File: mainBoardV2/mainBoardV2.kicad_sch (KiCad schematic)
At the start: 33 parts, among them J1 USB4125-GF-A_REVA2, SW1 SW_SPST, U1 ESP32-CAM, U2 ESP32-DEVKITC-32E, U3 MCP73871-2AAI_ML, U4 MPU6050_Module, U5 TPS61090RSARG4

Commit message: 3.6.26.C1
Wanted to start, but ended this session early
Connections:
- net +5V: no longer C4.1, R6.1, U3.17 (CE), U3.18 (IN), U3.19 (IN), U3.3 (SEL), U3.4 (PROG2), U3.9 (~{TE}), U7.4 (Common_Anode)
- net GND: no longer U6.2 (VBAT-)
- net at C6.1, U3.14 (VBAT), U3.15 (VBAT)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: no longer C1.1, L1.2, R1.1, U5.11 (EN), U5.8 (VBAT)
- new net: RintoCam1.2, RintoGyro1.2, SW1.1 (A), U2.J2_19 (EXT_5V)
- new net: C2.1, C3.1, R3.2, R5.1, U5.1 (VOUT), U5.15 (VOUT)
- new net: C1.1, L1.2, R1.1, U5.11 (EN), U5.8 (VBAT)
- new net: C4.1, R6.1, U3.17 (CE), U3.18 (IN), U3.19 (IN), U3.3 (SEL), U3.4 (PROG2), U3.9 (~{TE}), U7.4 (Common_Anode)
- new net: C5.1, U3.1 (OUT), U3.20 (OUT)
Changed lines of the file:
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@@
-	)
-	(junction
-		(at 160.02 62.23)
-		(diameter 0)
-		(color 0 0 0 0)
 	)
 	(junction
@@
 	)
 	(junction
-		(at 68.58 101.6)
-		(diameter 0)
-		(color 0 0 0 0)
-	)
-	(junction
 		(at 187.96 83.82)
 		(diameter 0)
@@
 	(junction
 		(at 115.57 156.21)
-		(diameter 0)
-		(color 0 0 0 0)
-	)
-	(junction
-		(at 41.91 167.64)
 		(diameter 0)
 		(color 0 0 0 0)
@@
 	(wire
 		(pts
-			(xy 154.94 156.21) (xy 154.94 62.23)
-		)
-		(stroke
-			(width 0)
-			(type default)
-		)
-	)
-	(wire
-		(pts
 			(xy 195.58 77.47) (xy 195.58 128.27)
 		)
@@
 	(wire
 		(pts
-			(xy 68.58 91.44) (xy 17.78 91.44)
-		)
-		(stroke
-			(width 0)
-			(type default)
-		)
-	)
-	(wire
-		(pts
 			(xy 73.66 114.3) (xy 76.2 114.3)
 		)
@@
 	(wire
 		(pts
-			(xy 68.58 101.6) (xy 76.2 101.6)
-		)
-		(stroke
-			(width 0)
-			(type default)
-		)
-	)
-	(wire
-		(pts
 			(xy 110.49 26.67) (xy 148.59 26.67)
 		)
@@
 	(wire
 		(pts
-			(xy 68.58 101.6) (xy 68.58 91.44)
-		)
-		(stroke
-			(width 0)
-			(type default)
-		)
-	)
-	(wire
-		(pts
 			(xy 185.42 67.31) (xy 195.58 67.31)
 		)
@@
 	(wire
 		(pts
-			(xy 21.59 167.64) (xy 41.91 167.64)
-		)
-		(stroke
-			(width 0)
-			(type default)
-		)
-	)
-	(wire
-		(pts
 			(xy 243.84 38.1) (xy 243.84 44.45)
 		)
@@
 	(wire
 		(pts
-			(xy 160.02 26.67) (xy 160.02 62.23)
-		)
-		(stroke
-			(width 0)
-			(type default)
-		)
-	)
-	(wire
-		(pts
 			(xy 110.49 33.02) (xy 134.62 33.02)
 		)
@@
 	(wire
 		(pts
-			(xy 17.78 91.44) (xy 17.78 26.67)
-		)
-		(stroke
-			(width 0)
-			(type default)
-		)
-	)
-	(wire
-		(pts
 			(xy 139.7 156.21) (xy 146.05 156.21)
 		)
@@
 	(wire
 		(pts
-			(xy 62.23 101.6) (xy 68.58 101.6)
+			(xy 62.23 101.6) (xy 76.2 101.6)
 		)
 		(stroke
@@
 	(wire
 		(pts
-			(xy 154.94 62.23) (xy 160.02 62.23)
-		)
-		(stroke
-			(width 0)
-			(type default)
-		)
-	)
-	(wire
-		(pts
 			(xy 74.93 60.96) (xy 74.93 64.77)
 		)
@@
 	(wire
 		(pts
-			(xy 41.91 120.65) (xy 41.91 160.02)
-		)
-		(stroke
-			(width 0)
-			(type default)
-		)
-	)
-	(wire
-		(pts
 			(xy 58.42 152.4) (xy 58.42 160.02)
 		)
@@
 	(wire
 		(pts
-			(xy 160.02 62.23) (xy 172.72 62.23)
-		)
-		(stroke
+			(xy 154.94 62.23) (xy 172.72 62.23)
+		)
+		(stroke

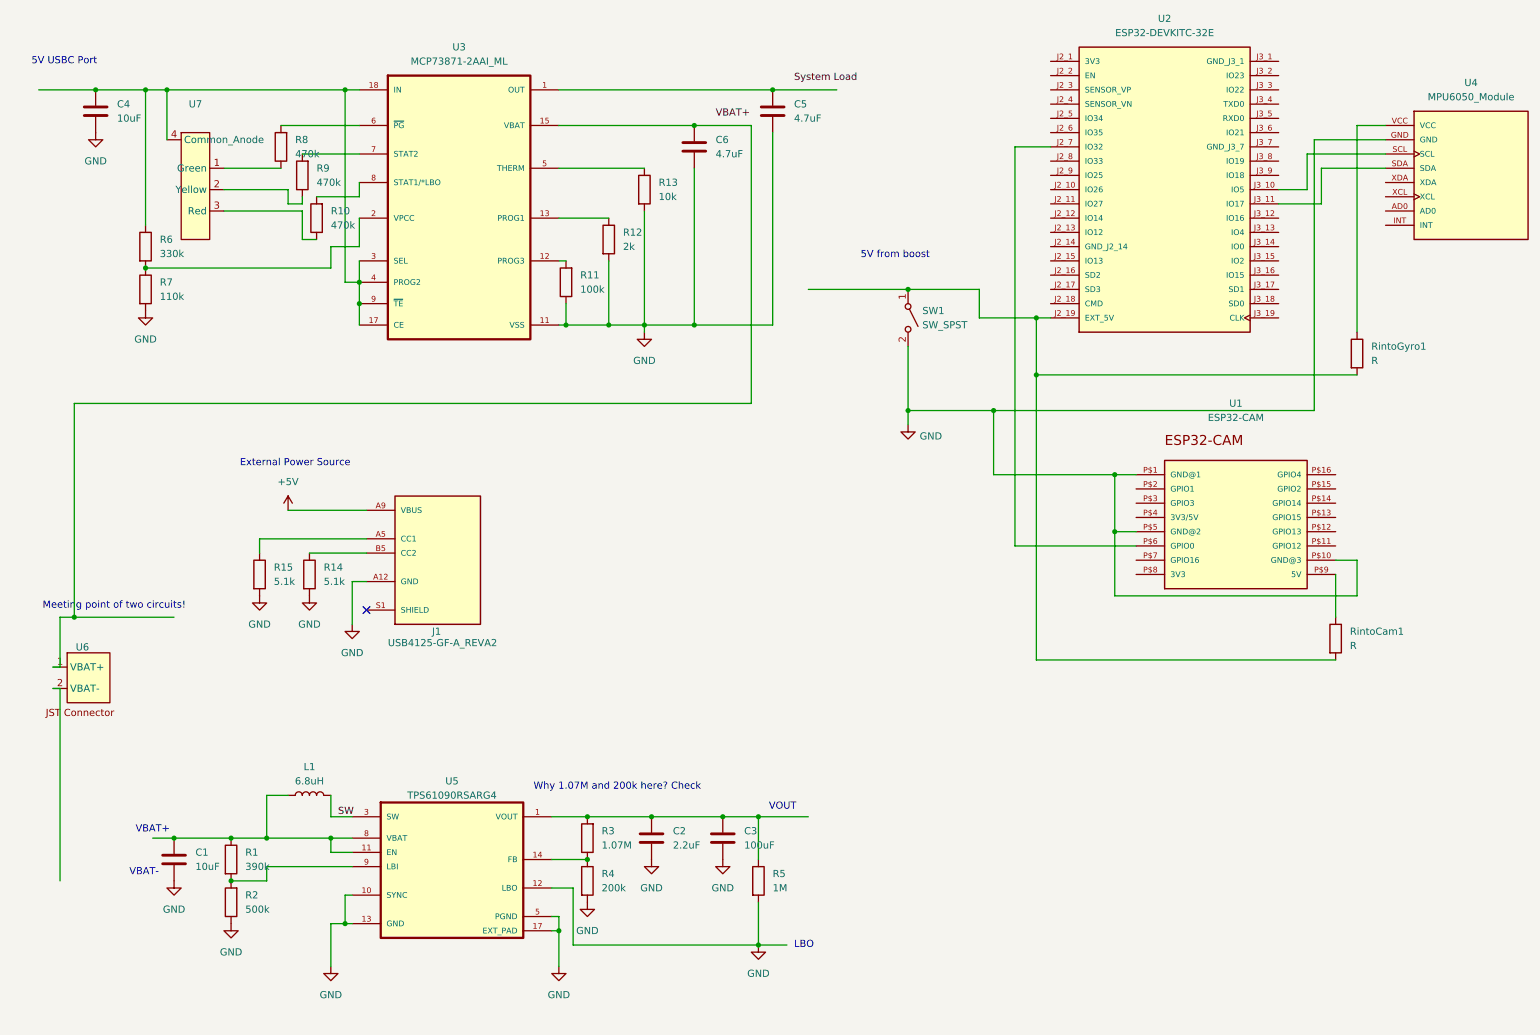
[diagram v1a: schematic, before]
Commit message: 3.7.26.C1
removed the old boost converter chip and circuit and put in the new one. Unconnected.
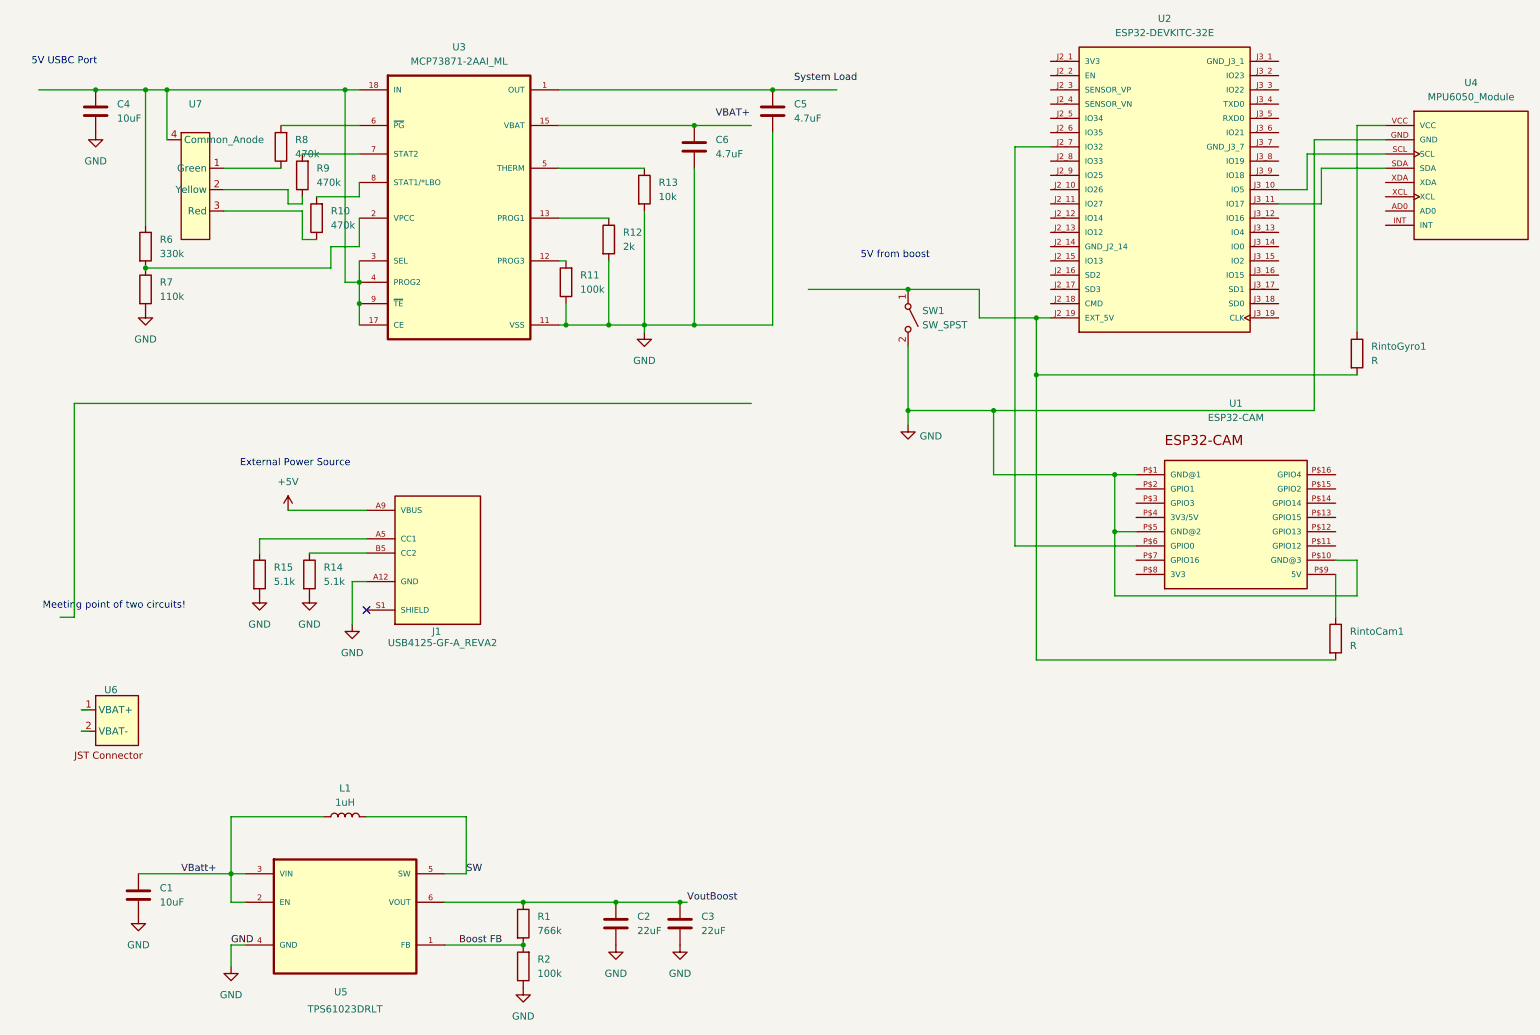
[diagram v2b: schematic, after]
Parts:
- removed R3: 1.07M, Resistor_SMD:R_0805_2012Metric_Pad1.20x1.40mm_HandSolder, symbol Device:R
- removed R4: 200k, Resistor_SMD:R_0805_2012Metric_Pad1.20x1.40mm_HandSolder, symbol Device:R
- removed R5: 1M, Resistor_SMD:R_0805_2012Metric_Pad1.20x1.40mm_HandSolder, symbol Device:R
- removed U5: TPS61090RSARG4, TPS61090RSARG4:QFN65P400X400X100-17N, symbol TPS61090RSARG4:TPS61090RSARG4
- added U5: TPS61023DRLT, TPS61023DRLT:SOT50P160X60-6N, symbol TPS61023DRLT:TPS61023DRLT
- C2: value 2.2uF -> 22uF
- C3: value 100uF -> 22uF; footprint T495C107K006ATE150(1):CAPMP6032X250 -> Capacitor_SMD:C_0805_2012Metric_Pad1.18x1.45mm_HandSolder
- L1: value 6.8uH -> 1uH
- R1: value 390k -> 766k
- R2: value 500k -> 100k
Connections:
- net GND: now also U5.4 (GND)
- net SW: now also U5.5 (SW)
- net at C6.1, U3.14 (VBAT), U3.15 (VBAT)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: no longer U6.1 (VBAT+)
- net VoutBoost: now reaches C2.1, C3.1
- net VoutBoost: now also R1.1, U5.6 (VOUT)
- net VBatt+: now reaches C1.1, L1.2
- net VBatt+: now also U5.2 (EN), U5.3 (VIN); no longer R1.1
- net Boost FB: now reaches R1.2, R2.2
- net Boost FB: now also U5.1 (FB)
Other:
- note removed: "LBO"
- note removed: "VBAT+"
- note removed: "VBAT-"
- note removed: "VOUT"
- note removed: "Why 1.07M and 200k here? Check"
- moved on the sheet: C1, C2, L1, R1, R2, U6

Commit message: 3.9.26.Cf
Closing the 3.9 session as it ran into 3.10. boost circuit ready to be optimally connected.

Charger ready for a fresh start.

Warning about 3 unconnected vias currently. Don't see them yet.
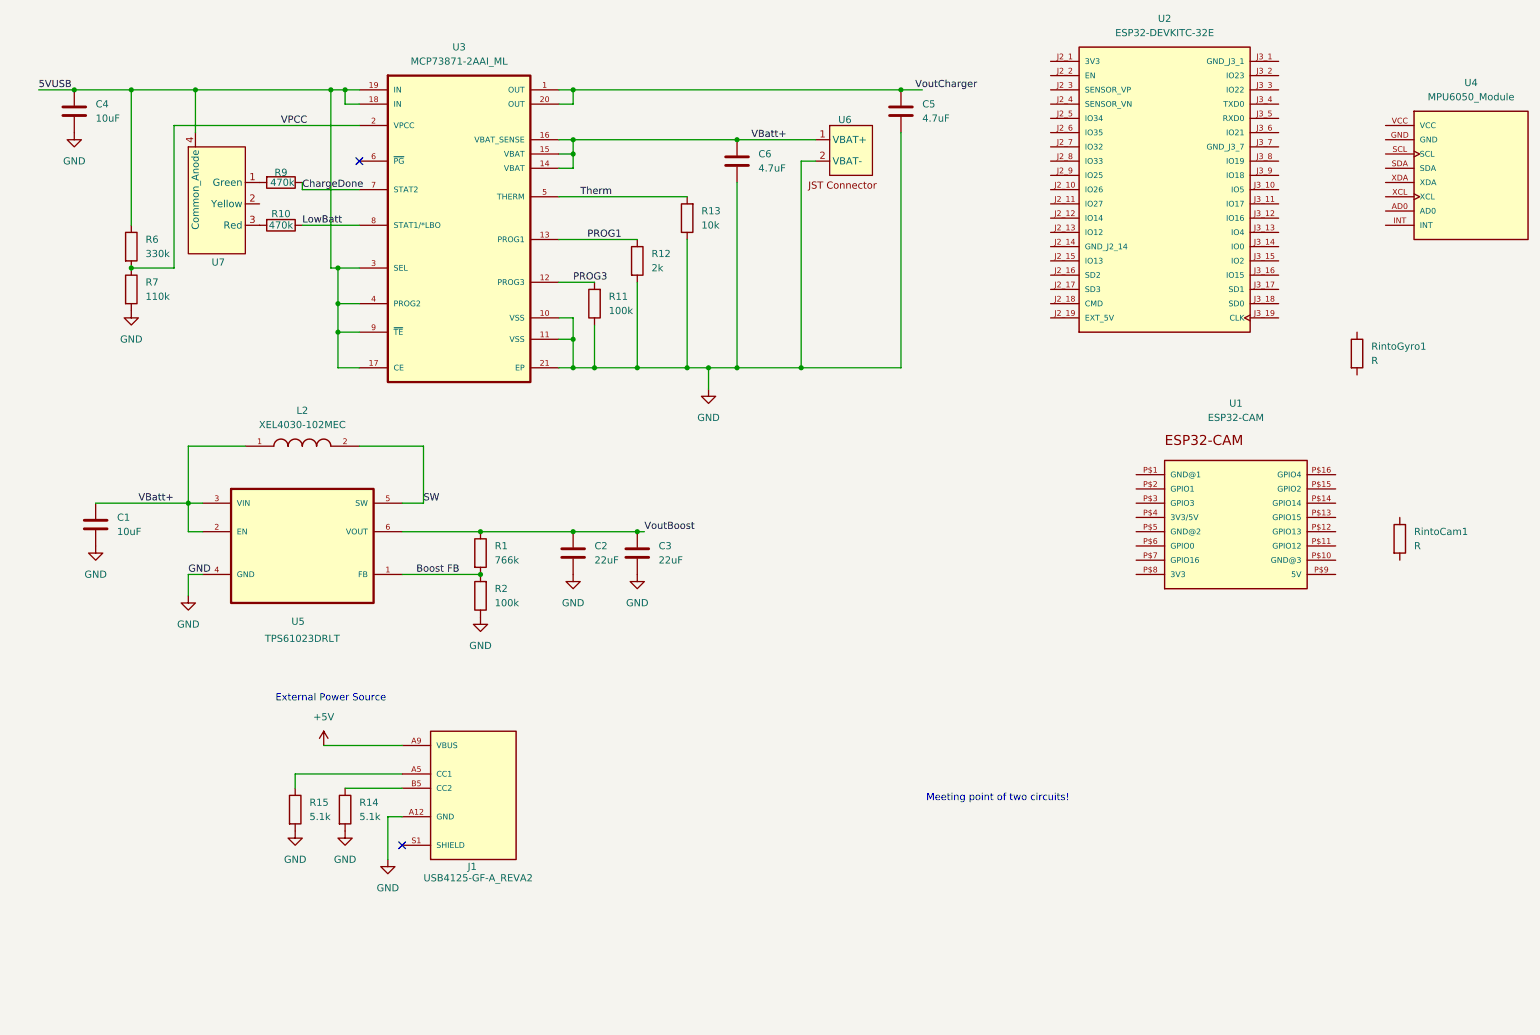
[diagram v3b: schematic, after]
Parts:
- removed L1: 1uH, Inductor_SMD:Sumida_senior, symbol Device:L
- removed R8: 470k, Resistor_SMD:R_0805_2012Metric_Pad1.20x1.40mm_HandSolder, symbol Device:R
- removed SW1: SW_SPST, symbol Switch:SW_SPST
- added L2: XEL4030-102MEC, XEL4030-102MEC:IND_XEL4030-102MEC, symbol XEL4030-102MEC:XEL4030-102MEC
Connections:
- net GND: now also R13.1, U6.2 (VBAT-); no longer R13.2, U1.P$1 (GND@1), U1.P$10 (GND@3), U1.P$5 (GND@2), U4.GND
- net SW: now also L2.2
- net VBatt+: now also C6.1, U3.14 (VBAT), U3.15 (VBAT), U3.16 (VBAT_SENSE), U6.1 (VBAT+), L2.1
- net PROG3: now reaches R11.2, U3.12 (PROG3)
- net at RintoCam1.1: no longer U1.P$9 (5V)
- net at U7.3 (Red): now also R10.2; no longer R10.1
- net LowBatt: now reaches U3.8 (STAT1/*LBO)
- net LowBatt: now also R10.1; no longer R10.2
- net Therm: now reaches U3.5 (THERM)
- net Therm: now also R13.2; no longer R13.1
- net 5VUSB: now reaches C4.1, R6.1, U3.17 (CE), U3.18 (IN), U3.19 (IN), U3.3 (SEL), U3.4 (PROG2), U3.9 (~{TE}), U7.4 (Common_Anode)
- net at U4.SCL: no longer U2.J3_10 (IO5)
- net at U4.SDA: no longer U2.J3_11 (IO17)
- net at U4.VCC: no longer RintoGyro1.1
- net VoutCharger: now reaches C5.1, U3.1 (OUT), U3.20 (OUT)
- net PROG1: now reaches R12.1, U3.13 (PROG1)
- net VPCC: now reaches R6.2, R7.1, U3.2 (VPCC)
- net at R9.2: now also U7.1 (Green); no longer U3.7 (STAT2)
- net at U1.P$6 (GPIO0): no longer U2.J2_7 (IO32)
- net at U7.2 (Yellow): no longer R9.1
- new net ChargeDone: R9.1, U3.7 (STAT2)
- now unconnected: RintoCam1.2, RintoGyro1.2, U2.J2_19 (EXT_5V)
- no-connect marks 1 -> 2
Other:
- note removed: "5V USBC Port"
- note removed: "5V from boost"
- moved on the sheet: C1, C2, C3, C4, C5, C6, J1, R1, R10, R11, R12, R13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

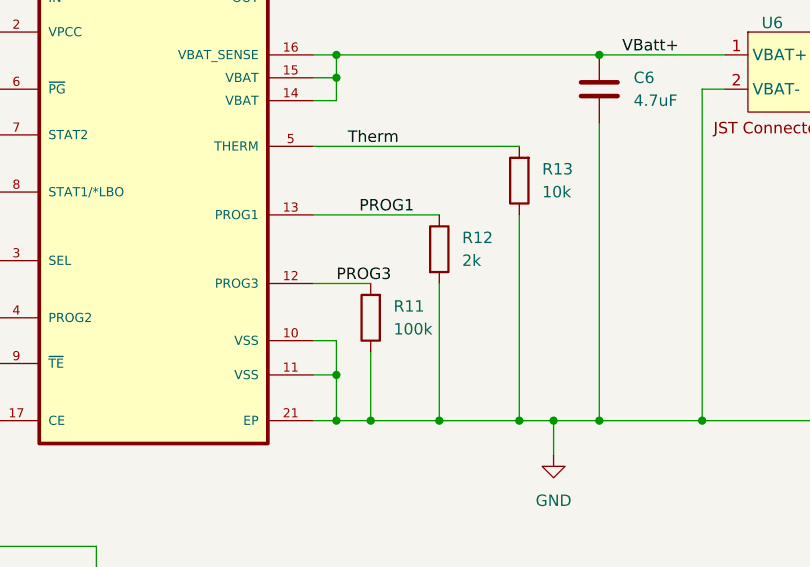
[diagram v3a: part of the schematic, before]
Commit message: 3.11.26.C2
Connected up the capacitors in the charging circuit.
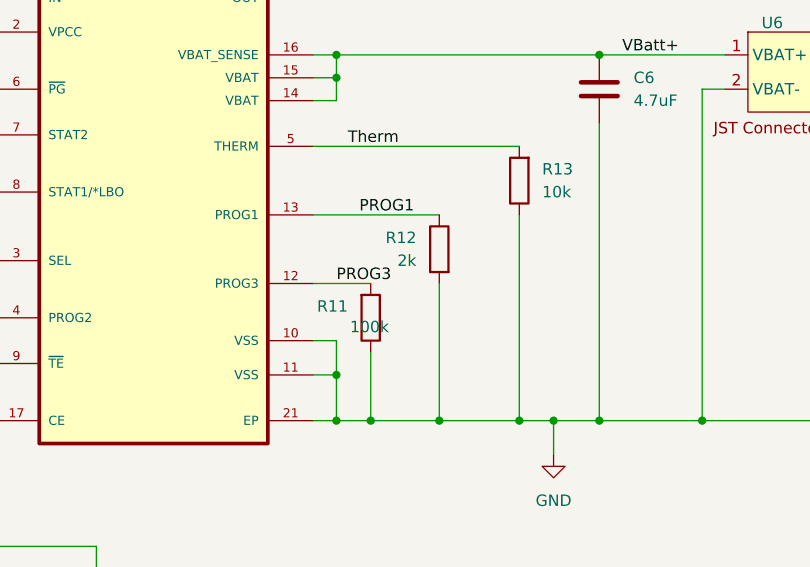
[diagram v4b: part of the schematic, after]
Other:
- moved on the sheet: R11
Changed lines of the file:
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@@
 	(symbol
 		(lib_id "Device:R")
-		(at 116.84 64.77 180)
+		(at 116.84 64.77 0)
+		(mirror x)
 		(unit 1)
 		(exclude_from_sim no)
@@
 		(on_board yes)
 		(dnp no)
-		(fields_autoplaced yes)
 		(property "Reference" "R11"
-			(at 119.38 63.4999 0)
+			(at 114.3 63.4999 0)
 			(effects
 				(font
@@
 		)
 		(property "Value" "100k"
-			(at 119.38 66.0399 0)
+			(at 118.872 65.786 0)
 			(effects
 				(font
@@
 		)
 		(property "Footprint" "Resistor_SMD:R_0805_2012Metric_Pad1.20x1.40mm_HandSolder"
-			(at 118.618 64.77 90)
+			(at 115.062 64.77 90)
 			(effects
 				(font
@@
 		(lib_id "Device:R")
 		(at 124.46 57.15 0)
+		(mirror y)
 		(unit 1)
 		(exclude_from_sim no)
@@
 		(on_board yes)
 		(dnp no)
-		(fields_autoplaced yes)
 		(property "Reference" "R12"
-			(at 127 55.8799 0)
+			(at 121.92 55.8799 0)
 			(effects
 				(font
@@
 		)
 		(property "Value" "2k"
-			(at 127 58.4199 0)
+			(at 121.92 58.4199 0)
 			(effects
 				(font
@@
 		)
 		(property "Footprint" "Resistor_SMD:R_0805_2012Metric_Pad1.20x1.40mm_HandSolder"
-			(at 122.682 57.15 90)
+			(at 126.238 57.15 90)
 			(effects
 				(font

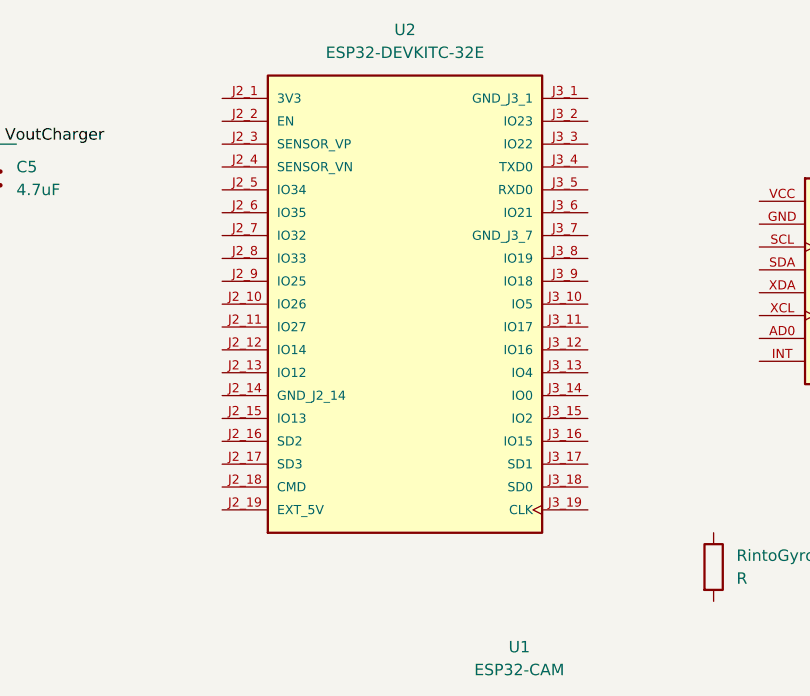
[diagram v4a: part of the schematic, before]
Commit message: 3.11.26.C3
Post meeting with Deepika and some group discussion, removing ESP32 from schemactic and breadboard. Moved some components closer together to get a rough estimate for board size so we can start designing a housing.
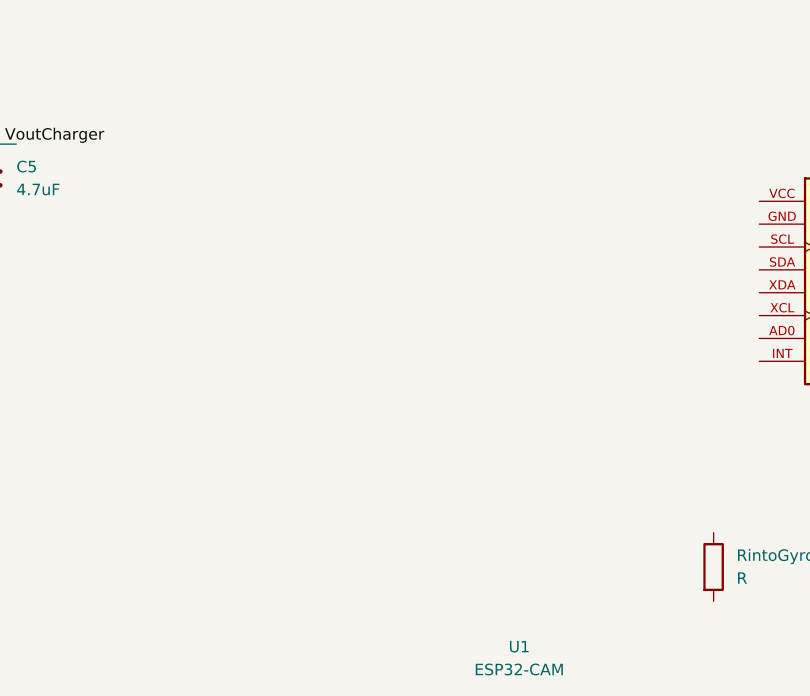
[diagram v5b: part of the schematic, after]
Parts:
- removed U2: ESP32-DEVKITC-32E, ESP32-DEVKITC-32E:MODULE_ESP32-DEVKITC-32E, symbol ESP32-DEVKITC-32E:ESP32-DEVKITC-32E
